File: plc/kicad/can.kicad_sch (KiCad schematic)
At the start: 1 part, among them CN2 DB2ERC-3.81-3P

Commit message: Added CAN circuit
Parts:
- removed CN2: DB2ERC-3.81-3P, LibrePLC32:CONN-TH_3P-P3.81_DB2ERC-3.81-3P, symbol LibrePLC32:DB2ERC-3.81-3P
- added C25: 100n, Capacitor_SMD:C_0805_2012Metric, symbol Device:C
- added C26: 1u, Capacitor_SMD:C_0805_2012Metric, symbol Device:C
- added CN6: DB2ERC-5.08-4P, LibrePLC32:CONN-TH_4P-P5.08_DB2ERC-5.08-4P, symbol LibrePLC32:DB2ERC-5.08-4P
- added D7: SM24CANA-02HTG, LibrePLC32:SOT-23_L2.9-W1.3-P1.90-LS2.4-BR, symbol LibrePLC32:SM24CANA-02HTG
- added R57: 120, Resistor_SMD:R_0805_2012Metric, symbol Device:R
- added SW2: MSK12C02, LibrePLC32:SW-TH_MSK12C02, symbol LibrePLC32:MSK12C02
- added U12: TCAN337DR, LibrePLC32:SOIC-8_L4.9-W3.9-P1.27-LS6.0-BL, symbol LibrePLC32:TCAN337DR
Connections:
- new net +3V3: C25.1, C26.1, U12.3 (VCC)
- new net +VSYS: CN6.1
- new net CAN_FAULT: U12.5 (FAULT)
- new net CAN_H: CN6.4, D7.1, R57.1, SW2.1, U12.7 (CANH)
- new net CAN_L: CN6.3, D7.2, R57.2, SW2.2, SW2.3, U12.6 (CANL)
- new net CAN_RX: U12.4 (RXD)
- new net CAN_TX: U12.1 (TXD)
- new net GND: C25.2, C26.2, CN6.2, D7.3, SW2.4, U12.2 (GND), U12.8 (S)

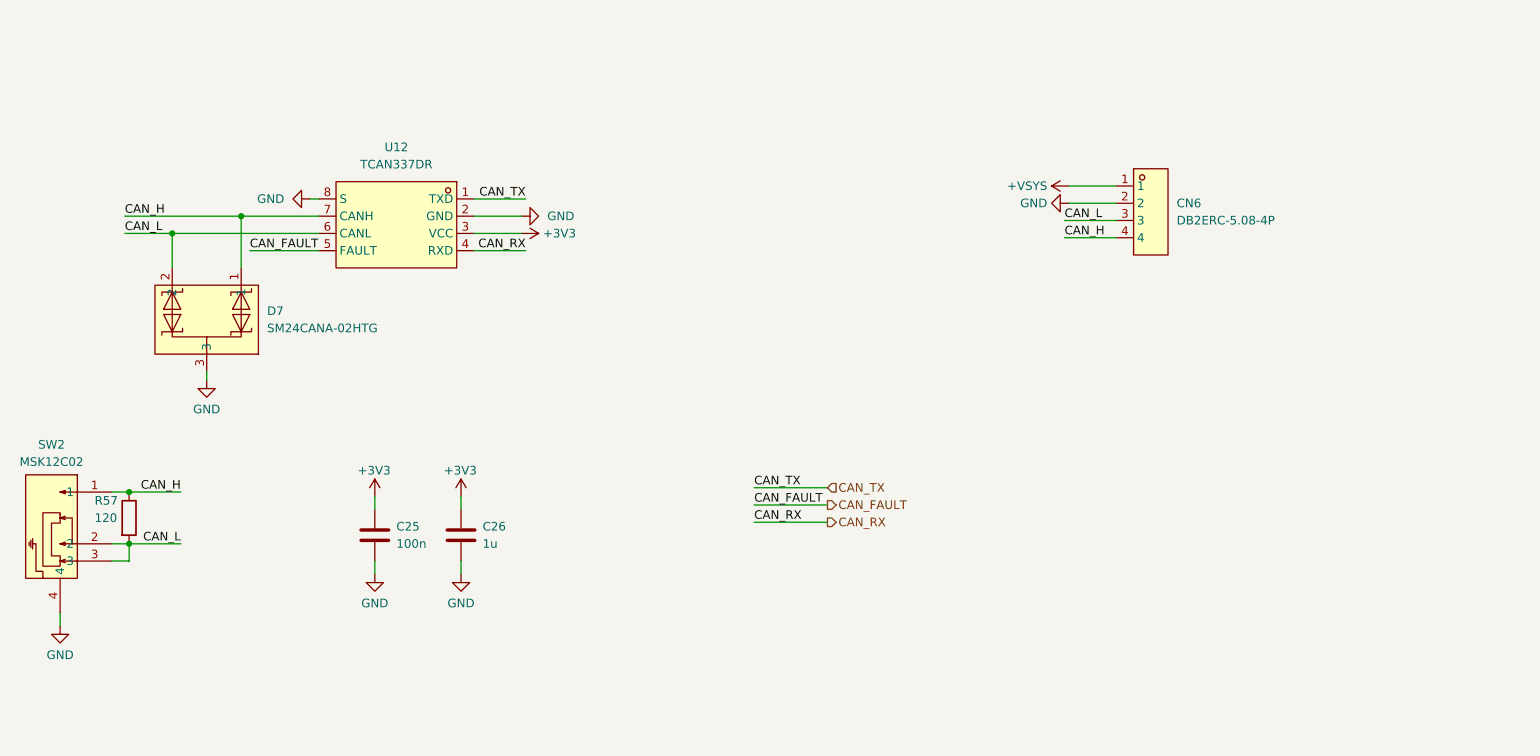
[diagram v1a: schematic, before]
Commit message: Added netclasses
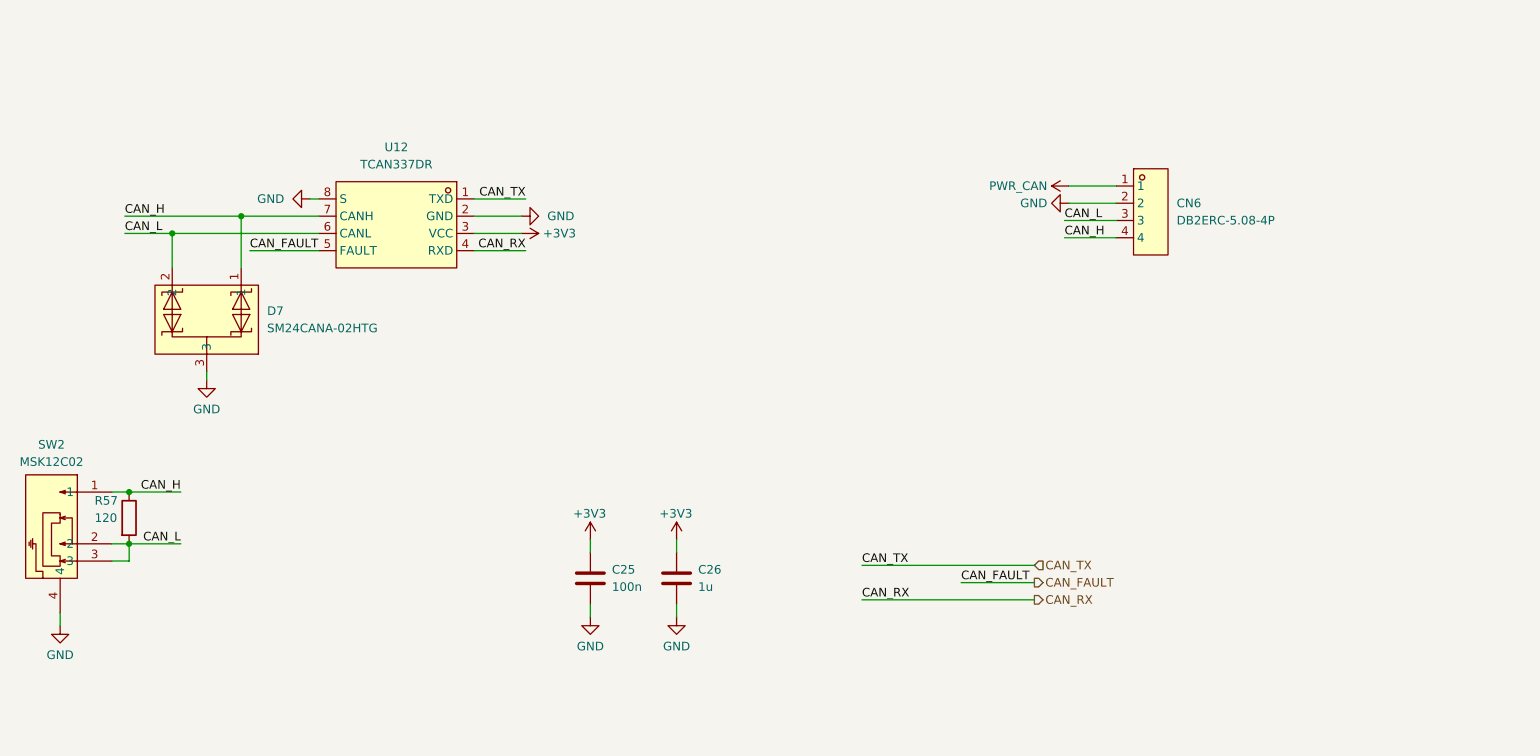
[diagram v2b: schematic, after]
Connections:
- net +VSYS renamed PWR_CAN
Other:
- moved on the sheet: C25, C26

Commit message: Added CP2102N bridge
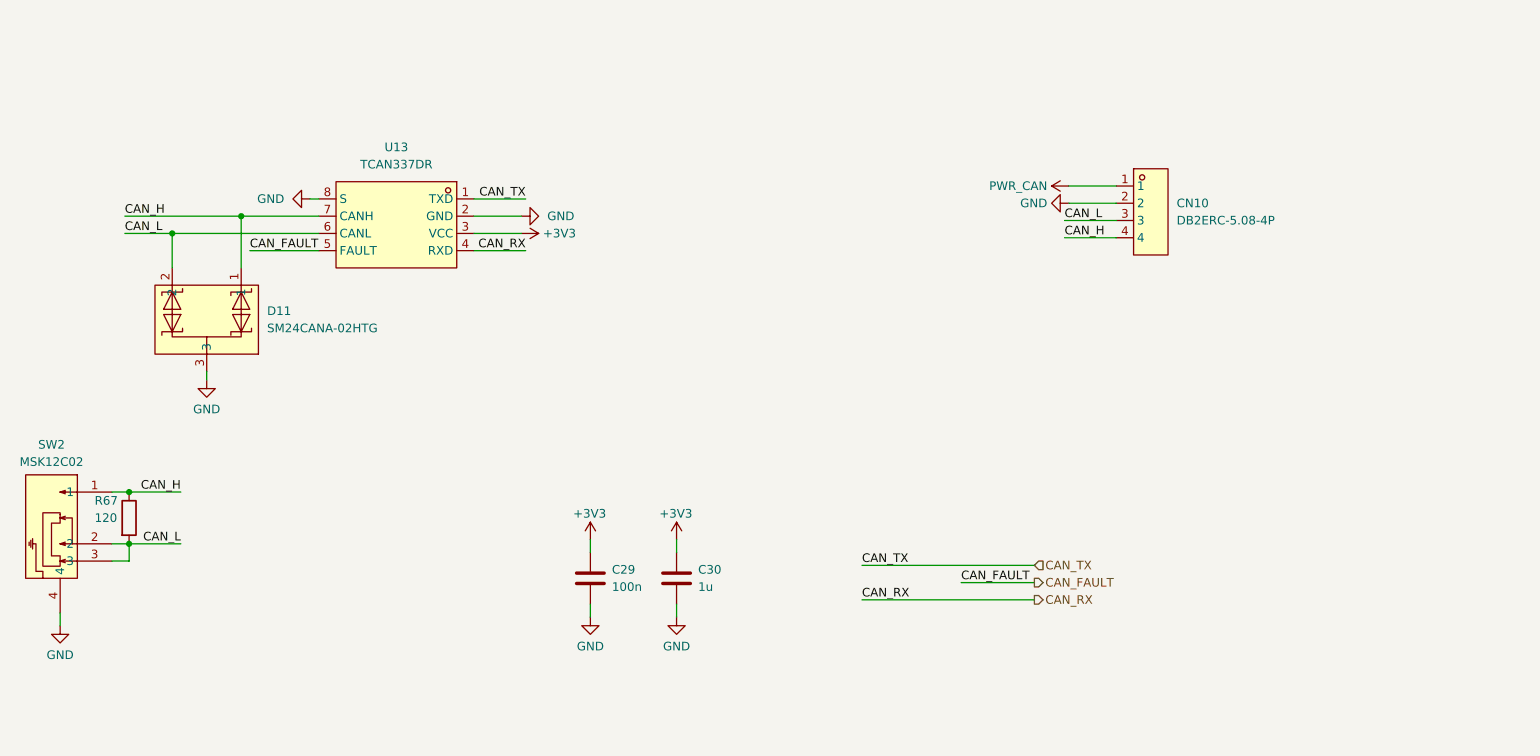
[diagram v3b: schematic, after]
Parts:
- renumbered C25 to C29, C26 to C30, CN6 to CN10, D7 to D11, R57 to R67, U12 to U13
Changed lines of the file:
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@@
 		(in_pos_files yes)
 		(dnp no)
-		(property "Reference" "#PWR0136"
+		(property "Reference" "#PWR0131"
 			(at 133.985 140.335 0)
 			(hide yes)
@@
 			(project "LibrePLC32"
 				(path "/ef4c1a27-85a3-413a-9f93-a41c4f97eee5/1f15b1b2-5031-4e14-8391-148d71dbf666"
-					(reference "#PWR0136")
+					(reference "#PWR0131")
 					(unit 1)
 				)
@@
 		(dnp no)
 		(fields_autoplaced yes)
-		(property "Reference" "#PWR0137"
+		(property "Reference" "#PWR0132"
 			(at 133.985 154.305 0)
 			(hide yes)
@@
 			(project "LibrePLC32"
 				(path "/ef4c1a27-85a3-413a-9f93-a41c4f97eee5/1f15b1b2-5031-4e14-8391-148d71dbf666"
-					(reference "#PWR0137")
+					(reference "#PWR0132")
 					(unit 1)
 				)
@@
 		(in_pos_files yes)
 		(dnp no)
-		(property "Reference" "#PWR0139"
+		(property "Reference" "#PWR0126"
 			(at 73.66 86.36 0)
 			(hide yes)
@@
 			(project "LibrePLC32"
 				(path "/ef4c1a27-85a3-413a-9f93-a41c4f97eee5/1f15b1b2-5031-4e14-8391-148d71dbf666"
-					(reference "#PWR0139")
+					(reference "#PWR0126")
 					(unit 1)
 				)
@@
 		(dnp no)
 		(fields_autoplaced yes)
-		(property "Reference" "#PWR0132"
+		(property "Reference" "#PWR0124"
 			(at 43.18 155.575 0)
 			(hide yes)
@@
 			(project "LibrePLC32"
 				(path "/ef4c1a27-85a3-413a-9f93-a41c4f97eee5/1f15b1b2-5031-4e14-8391-148d71dbf666"
-					(reference "#PWR0132")
+					(reference "#PWR0124")
 					(unit 1)
 				)
@@
 		(dnp no)
 		(fields_autoplaced yes)
-		(property "Reference" "D7"
+		(property "Reference" "D11"
 			(at 73.66 102.8699 0)
 			(show_name no)
@@
 			(project "LibrePLC32"
 				(path "/ef4c1a27-85a3-413a-9f93-a41c4f97eee5/1f15b1b2-5031-4e14-8391-148d71dbf666"
-					(reference "D7")
+					(reference "D11")
 					(unit 1)
 				)
@@
 		(in_pos_files yes)
 		(dnp no)
-		(property "Reference" "#PWR0133"
+		(property "Reference" "#PWR0128"
 			(at 107.315 91.44 0)
 			(hide yes)
@@
 			(project "LibrePLC32"
 				(path "/ef4c1a27-85a3-413a-9f93-a41c4f97eee5/1f15b1b2-5031-4e14-8391-148d71dbf666"
-					(reference "#PWR0133")
+					(reference "#PWR0128")
 					(unit 1)
 				)
@@
 		(dnp no)
 		(fields_autoplaced yes)
-		(property "Reference" "C25"
+		(property "Reference" "C29"
 			(at 124.46 140.9699 0)
 			(show_name no)
@@
 			(project "LibrePLC32"
 				(path "/ef4c1a27-85a3-413a-9f93-a41c4f97eee5/1f15b1b2-5031-4e14-8391-148d71dbf666"
-					(reference "C25")
+					(reference "C29")
 					(unit 1)
 				)
@@
 		(in_pos_files yes)
 		(dnp no)
-		(property "Reference" "#PWR0131"
+		(property "Reference" "#PWR0127"
 			(at 117.475 88.9 0)
 			(hide yes)
@@
 			(project "LibrePLC32"
 				(path "/ef4c1a27-85a3-413a-9f93-a41c4f97eee5/1f15b1b2-5031-4e14-8391-148d71dbf666"
-					(reference "#PWR0131")
+					(reference "#PWR0127")
 					(unit 1)
 				)
@@
 		(in_pos_files yes)
 		(dnp no)
-		(property "Reference" "R57"
+		(property "Reference" "R67"
 			(at 48.26 130.81 0)
 			(show_name no)
@@
 			(project "LibrePLC32"
 				(path "/ef4c1a27-85a3-413a-9f93-a41c4f97eee5/1f15b1b2-5031-4e14-8391-148d71dbf666"
-					(reference "R57")
+					(reference "R67")
 					(unit 1)
 				)
@@
 		(dnp no)
 		(fields_autoplaced yes)
-		(property "Reference" "C26"
+		(property "Reference" "C30"
 			(at 137.16 140.9699 0)
 			(show_name no)
@@
 			(project "LibrePLC32"
 				(path "/ef4c1a27-85a3-413a-9f93-a41c4f97eee5/1f15b1b2-5031-4e14-8391-148d71dbf666"
-					(reference "C26")
+					(reference "C30")
 					(unit 1)
 				)
@@
 		(in_pos_files yes)
 		(dnp no)
-		(property "Reference" "U12"
+		(property "Reference" "U13"
 			(at 92.71 78.74 0)
 			(show_name no)
@@
 			(project "LibrePLC32"
 				(path "/ef4c1a27-85a3-413a-9f93-a41c4f97eee5/1f15b1b2-5031-4e14-8391-148d71dbf666"
-					(reference "U12")
+					(reference "U13")
 					(unit 1)
 				)
@@
 		(dnp no)
 		(fields_autoplaced yes)
-		(property "Reference" "#PWR0150"
+		(property "Reference" "#PWR0133"
 			(at 195.58 84.455 0)
 			(hide yes)
@@
 			(project "LibrePLC32"
 				(path "/ef4c1a27-85a3-413a-9f93-a41c4f97eee5/1f15b1b2-5031-4e14-8391-148d71dbf666"
-					(reference "#PWR0150")
+					(reference "#PWR0133")
 					(unit 1)
 				)
@@
 		(dnp no)
 		(fields_autoplaced yes)
-		(property "Reference" "#PWR0138"
+		(property "Reference" "#PWR0125"
 			(at 64.77 119.38 0)
 			(hide yes)
@@
 			(project "LibrePLC32"
 				(path "/ef4c1a27-85a3-413a-9f93-a41c4f97eee5/1f15b1b2-5031-4e14-8391-148d71dbf666"
-					(reference "#PWR0138")
+					(reference "#PWR0125")
 					(unit 1)
 				)
@@
 		(dnp no)
 		(fields_autoplaced yes)
-		(property "Reference" "CN6"
+		(property "Reference" "CN10"
 			(at 207.645 86.9949 0)
 			(show_name no)
@@
 			(project "LibrePLC32"
 				(path "/ef4c1a27-85a3-413a-9f93-a41c4f97eee5/1f15b1b2-5031-4e14-8391-148d71dbf666"
-					(reference "CN6")
-					(unit 1)
-				)
+					(reference "CN10")
+					(unit 1)
+				)

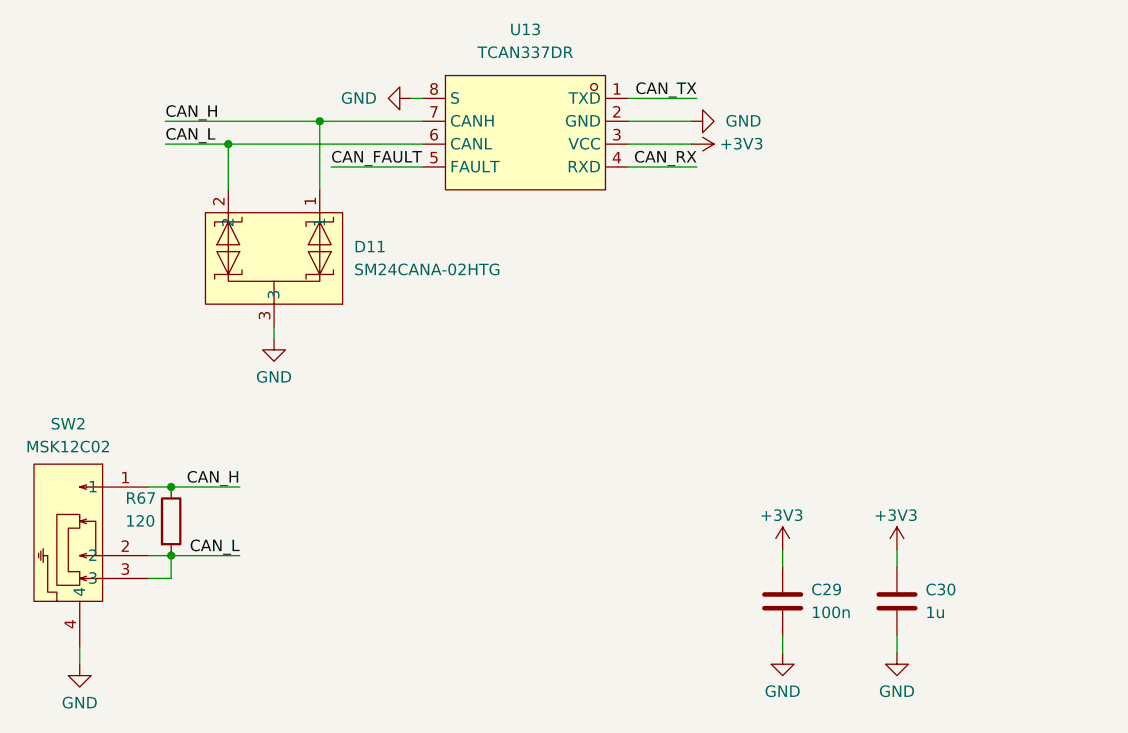
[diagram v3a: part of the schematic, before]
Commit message: Added 3.3V regulator
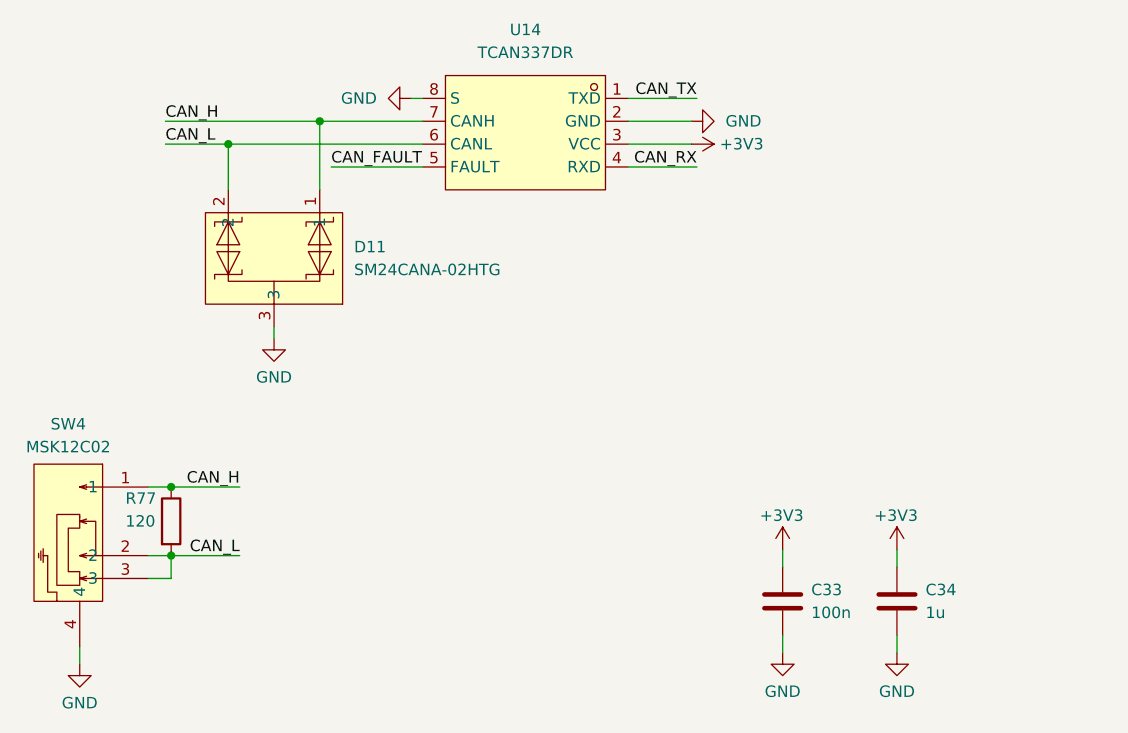
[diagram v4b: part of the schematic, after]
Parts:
- renumbered C29 to C33, C30 to C34, R67 to R77, SW2 to SW4, U13 to U14
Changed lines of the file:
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@@
 		(in_pos_files yes)
 		(dnp no)
-		(property "Reference" "#PWR0131"
+		(property "Reference" "#PWR0160"
 			(at 133.985 140.335 0)
 			(hide yes)
@@
 			(project "LibrePLC32"
 				(path "/ef4c1a27-85a3-413a-9f93-a41c4f97eee5/1f15b1b2-5031-4e14-8391-148d71dbf666"
-					(reference "#PWR0131")
+					(reference "#PWR0160")
 					(unit 1)
 				)
@@
 		(dnp no)
 		(fields_autoplaced yes)
-		(property "Reference" "#PWR0132"
+		(property "Reference" "#PWR0161"
 			(at 133.985 154.305 0)
 			(hide yes)
@@
 			(project "LibrePLC32"
 				(path "/ef4c1a27-85a3-413a-9f93-a41c4f97eee5/1f15b1b2-5031-4e14-8391-148d71dbf666"
-					(reference "#PWR0132")
+					(reference "#PWR0161")
 					(unit 1)
 				)
@@
 		(in_pos_files yes)
 		(dnp no)
-		(property "Reference" "#PWR0126"
+		(property "Reference" "#PWR0155"
 			(at 73.66 86.36 0)
 			(hide yes)
@@
 			(project "LibrePLC32"
 				(path "/ef4c1a27-85a3-413a-9f93-a41c4f97eee5/1f15b1b2-5031-4e14-8391-148d71dbf666"
-					(reference "#PWR0126")
+					(reference "#PWR0155")
 					(unit 1)
 				)
@@
 		(dnp no)
 		(fields_autoplaced yes)
-		(property "Reference" "SW2"
+		(property "Reference" "SW4"
 			(at 41.91 122.555 90)
 			(show_name no)
@@
 			(project "LibrePLC32"
 				(path "/ef4c1a27-85a3-413a-9f93-a41c4f97eee5/1f15b1b2-5031-4e14-8391-148d71dbf666"
-					(reference "SW2")
+					(reference "SW4")
 					(unit 1)
 				)
@@
 		(dnp no)
 		(fields_autoplaced yes)
-		(property "Reference" "#PWR0124"
+		(property "Reference" "#PWR0153"
 			(at 43.18 155.575 0)
 			(hide yes)
@@
 			(project "LibrePLC32"
 				(path "/ef4c1a27-85a3-413a-9f93-a41c4f97eee5/1f15b1b2-5031-4e14-8391-148d71dbf666"
-					(reference "#PWR0124")
+					(reference "#PWR0153")
 					(unit 1)
 				)
@@
 		(in_pos_files yes)
 		(dnp no)
-		(property "Reference" "#PWR0128"
+		(property "Reference" "#PWR0157"
 			(at 107.315 91.44 0)
 			(hide yes)
@@
 			(project "LibrePLC32"
 				(path "/ef4c1a27-85a3-413a-9f93-a41c4f97eee5/1f15b1b2-5031-4e14-8391-148d71dbf666"
-					(reference "#PWR0128")
+					(reference "#PWR0157")
 					(unit 1)
 				)
@@
 		(dnp no)
 		(fields_autoplaced yes)
-		(property "Reference" "C29"
+		(property "Reference" "C33"
 			(at 124.46 140.9699 0)
 			(show_name no)
@@
 			(project "LibrePLC32"
 				(path "/ef4c1a27-85a3-413a-9f93-a41c4f97eee5/1f15b1b2-5031-4e14-8391-148d71dbf666"
-					(reference "C29")
+					(reference "C33")
 					(unit 1)
 				)
@@
 		(in_pos_files yes)
 		(dnp no)
-		(property "Reference" "#PWR0127"
+		(property "Reference" "#PWR0156"
 			(at 117.475 88.9 0)
 			(hide yes)
@@
 			(project "LibrePLC32"
 				(path "/ef4c1a27-85a3-413a-9f93-a41c4f97eee5/1f15b1b2-5031-4e14-8391-148d71dbf666"
-					(reference "#PWR0127")
+					(reference "#PWR0156")
 					(unit 1)
 				)
@@
 		(in_pos_files yes)
 		(dnp no)
-		(property "Reference" "R67"
+		(property "Reference" "R77"
 			(at 48.26 130.81 0)
 			(show_name no)
@@
 			(project "LibrePLC32"
 				(path "/ef4c1a27-85a3-413a-9f93-a41c4f97eee5/1f15b1b2-5031-4e14-8391-148d71dbf666"
-					(reference "R67")
+					(reference "R77")
 					(unit 1)
 				)
@@
 		(dnp no)
 		(fields_autoplaced yes)
-		(property "Reference" "C30"
+		(property "Reference" "C34"
 			(at 137.16 140.9699 0)
 			(show_name no)
@@
 			(project "LibrePLC32"
 				(path "/ef4c1a27-85a3-413a-9f93-a41c4f97eee5/1f15b1b2-5031-4e14-8391-148d71dbf666"
-					(reference "C30")
+					(reference "C34")
 					(unit 1)
 				)
@@
 		(dnp no)
 		(fields_autoplaced yes)
-		(property "Reference" "#PWR0134"
+		(property "Reference" "#PWR0163"
 			(at 185.42 86.995 0)
 			(hide yes)
@@
 			(project "LibrePLC32"
 				(path "/ef4c1a27-85a3-413a-9f93-a41c4f97eee5/1f15b1b2-5031-4e14-8391-148d71dbf666"
-					(reference "#PWR0134")
+					(reference "#PWR0163")
 					(unit 1)
 				)
@@
 		(dnp no)
 		(fields_autoplaced yes)
-		(property "Reference" "#PWR0130"
+		(property "Reference" "#PWR0159"
 			(at 121.285 154.305 0)
 			(hide yes)
@@
 			(project "LibrePLC32"
 				(path "/ef4c1a27-85a3-413a-9f93-a41c4f97eee5/1f15b1b2-5031-4e14-8391-148d71dbf666"
-					(reference "#PWR0130")
+					(reference "#PWR0159")
 					(unit 1)
 				)
@@
 		(in_pos_files yes)
 		(dnp no)
-		(property "Reference" "U13"
+		(property "Reference" "U14"
 			(at 92.71 78.74 0)
 			(show_name no)
@@
 			(project "LibrePLC32"
 				(path "/ef4c1a27-85a3-413a-9f93-a41c4f97eee5/1f15b1b2-5031-4e14-8391-148d71dbf666"
-					(reference "U13")
+					(reference "U14")
 					(unit 1)
 				)
@@
 		(dnp no)
 		(fields_autoplaced yes)
-		(property "Reference" "#PWR0133"
+		(property "Reference" "#PWR0162"
 			(at 195.58 84.455 0)
 			(hide yes)
@@
 			(project "LibrePLC32"
 				(path "/ef4c1a27-85a3-413a-9f93-a41c4f97eee5/1f15b1b2-5031-4e14-8391-148d71dbf666"
-					(reference "#PWR0133")
+					(reference "#PWR0162")
 					(unit 1)
 				)
@@
 		(dnp no)
 		(fields_autoplaced yes)
-		(property "Reference" "#PWR0125"
+		(property "Reference" "#PWR0154"
 			(at 64.77 119.38 0)
 			(hide yes)
@@
 			(project "LibrePLC32"
 				(path "/ef4c1a27-85a3-413a-9f93-a41c4f97eee5/1f15b1b2-5031-4e14-8391-148d71dbf666"
-					(reference "#PWR0125")
+					(reference "#PWR0154")
 					(unit 1)
 				)
@@
 		(in_pos_files yes)
 		(dnp no)
-		(property "Reference" "#PWR0129"
+		(property "Reference" "#PWR0158"
 			(at 121.285 140.335 0)
 			(hide yes)
@@
 			(project "LibrePLC32"
 				(path "/ef4c1a27-85a3-413a-9f93-a41c4f97eee5/1f15b1b2-5031-4e14-8391-148d71dbf666"
-					(reference "#PWR0129")
-					(unit 1)
-				)
+					(reference "#PWR0158")
+					(unit 1)
+				)
